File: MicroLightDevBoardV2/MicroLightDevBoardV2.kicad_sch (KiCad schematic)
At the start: 84 parts, among them J1 Conn_01x05_Socket, J10 Conn_01x02_Socket, J11 Conn_01x05_Socket, J12 Conn_01x02_Socket, J13 Conn_01x04_Socket, J14 Conn_01x04_Socket, J15 Conn_01x05_Socket, J16 Conn_01x02_Socket, J17 Conn_01x04_Socket, J18 Conn_01x02_Socket, J19 Conn_01x02_Socket, J2 Conn_01x05_Socket, J20 Conn_01x04_Socket, J21 Conn_01x04_Socket, J22 Conn_01x02_Socket, J23 Conn_01x02_Socket, J24 Conn_01x02_Socket, J25 Conn_01x02_Socket, J26 Conn_01x02_Socket, J27 Conn_01x04_Socket, J28 Conn_01x02_Socket, J29 Conn_01x04_Socket, J3 Conn_01x05_Socket, J30 Conn_01x04_Socket, J31 Conn_01x04_Socket, J32 Conn_01x04_Socket, J33 Conn_01x04_Socket, J34 Conn_01x04_Socket, J35 Conn_01x04_Socket, J36 Conn_01x04_Socket, J37 Conn_01x04_Socket, J38 Conn_01x04_Socket, J39 Conn_01x04_Socket, J4 Conn_01x05_Socket, J40 Conn_01x04_Socket, J41 Conn_01x04_Socket, J42 Conn_01x04_Socket, J43 Conn_01x04_Socket, J44 Conn_01x04_Socket, J45 Conn_01x04_Socket, J46 Conn_01x04_Socket, J47 Conn_01x04_Socket, J48 Conn_01x04_Socket, J49 Conn_01x04_Socket, J5 Conn_01x02_Socket, J50 Conn_01x04_Socket, J6 Conn_01x02_Socket, J7 TYPE-C-31-M-12, J8 Conn_01x02_Socket, J9 Conn_01x02_Socket, U1 BQ25628RYKR, U2 ATtiny3226-M, U3 S-85S1AB33-I6T1U, U4 B3U-1000P, U5 B3U-1000P, U6 USBLC6-2P6, U7 MC3479

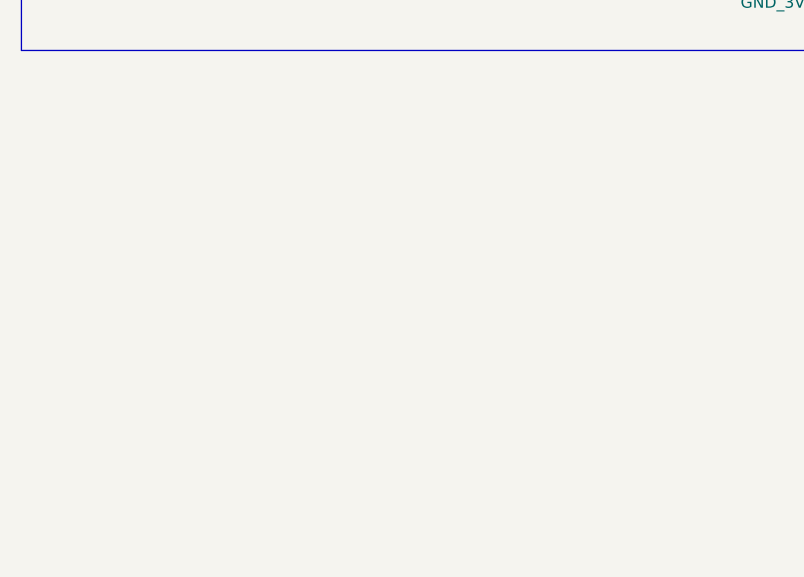
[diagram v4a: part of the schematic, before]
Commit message: added linear charging ic from TI
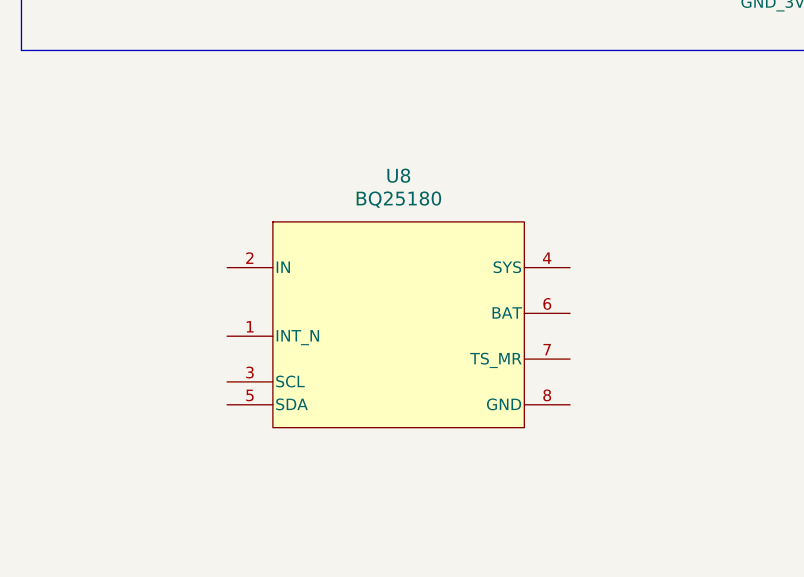
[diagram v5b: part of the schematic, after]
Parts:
- added U8: BQ25180, MicroLightDevBoard:BQ25180, symbol MicroLightDevBoard:BQ25180
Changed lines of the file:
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@@
+	)
+	(symbol
+		(lib_id "MicroLightDevBoard:BQ25180")
+		(at 38.1 213.36 0)
+		(unit 1)
+		(exclude_from_sim no)
+		(in_bom yes)
+		(on_board yes)
+		(dnp no)
+		(fields_autoplaced yes)
+		(property "Reference" "U8"
+			(at 57.15 203.2 0)
+			(effects
+				(font
+					(size 1.524 1.524)
+				)
+			)
+		)
+		(property "Value" "BQ25180"
+			(at 57.15 205.74 0)
+			(effects
+				(font
+					(size 1.524 1.524)
+				)
+			)
+		)
+		(property "Footprint" "MicroLightDevBoard:BQ25180"
+			(at 74.676 203.708 0)
+			(effects
+				(font
+					(size 1.27 1.27)
+					(italic yes)
+				)
+				(hide yes)
+			)
+		)
+		(property "Datasheet" "BQ25180"
+			(at 56.134 203.454 0)
+			(effects
+				(font
+					(size 1.27 1.27)
+					(italic yes)
+				)
+				(hide yes)
+			)
+		)
+		(property "Description" "https://www.ti.com/lit/ds/symlink/bq25180.pdf"
+			(at 57.404 198.628 0)
+			(effects
+				(font
+					(size 1.27 1.27)
+				)
+				(hide yes)
+			)
+		)
+		(pin "4"
+		)
+		(pin "7"
+		)
+		(pin "5"
+		)
+		(pin "6"
+		)
+		(pin "8"
+		)
+		(pin "3"
+		)
+		(pin "1"
+		)
+		(pin "2"
+		)
+		(instances
+			(project ""
+				(path "/4d4b60a6-56d4-4632-90b9-cd9e4f577154"
+					(reference "U8")
+					(unit 1)
+				)
+			)
+		)
 	)
 	(symbol
@@
 			)
 		)
-		(property "Datasheet" "S-85S1AB33-I6T1U"
+		(property "Datasheet" "https://www.mouser.com/datasheet/2/1490/S85S1A_E-3431038.pdf"
 			(at 57.15 168.91 0)
 			(effects

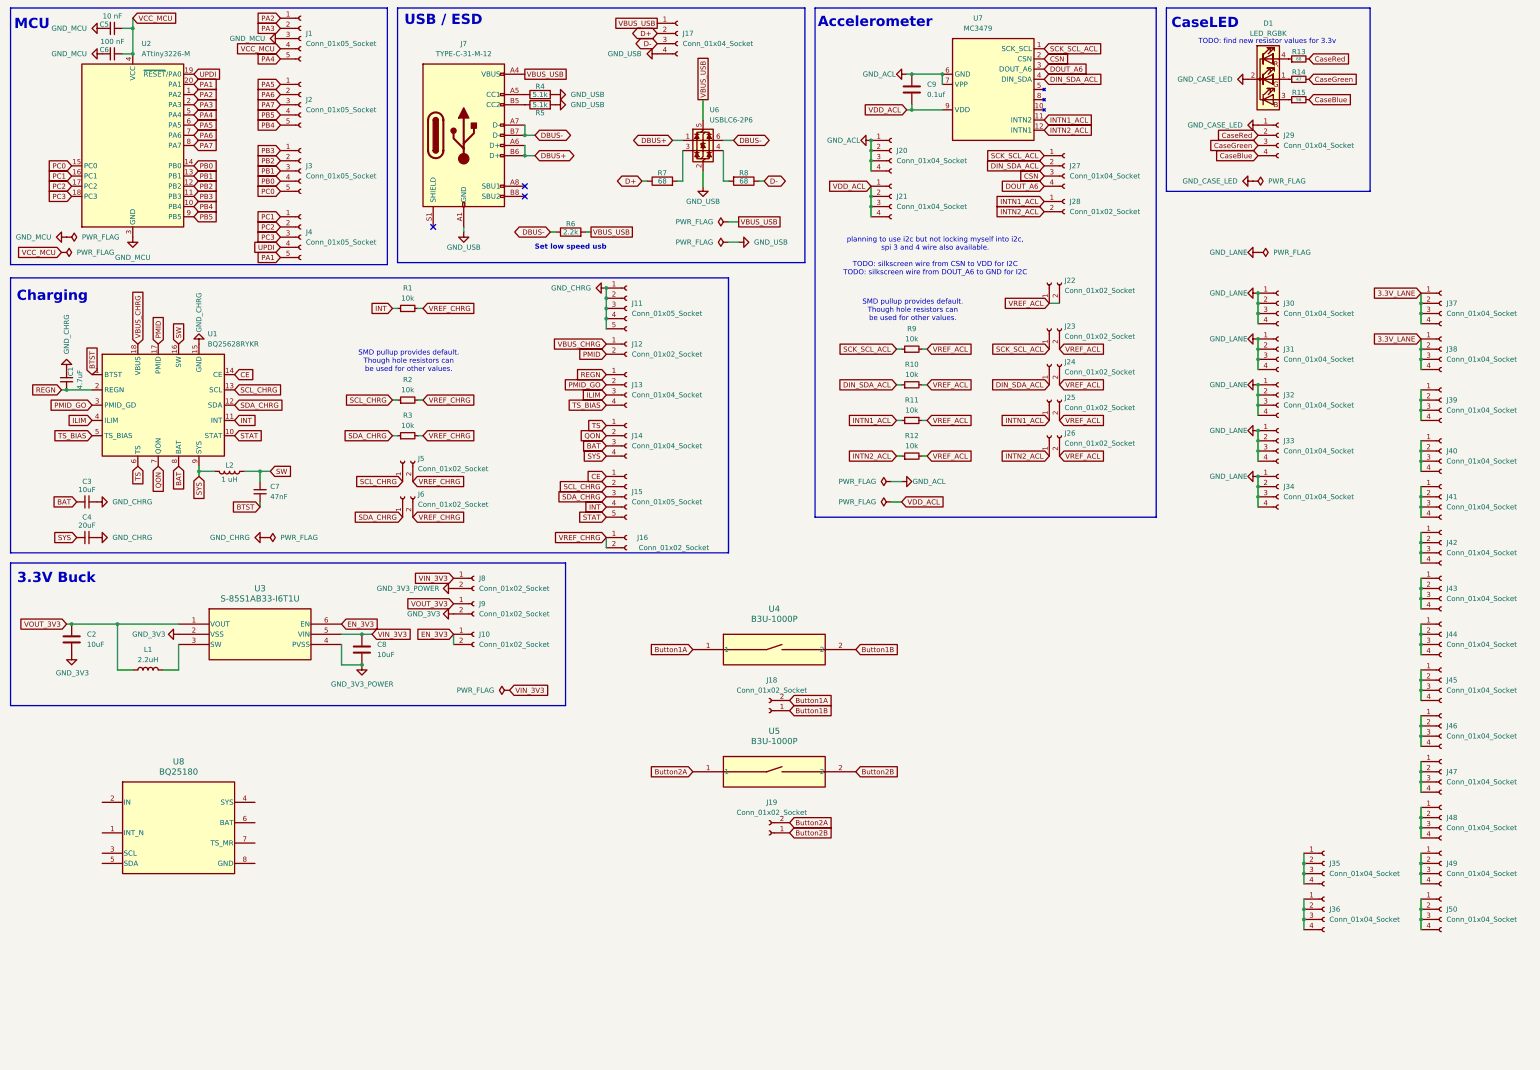
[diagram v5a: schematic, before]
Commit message: added connections for new charger ic
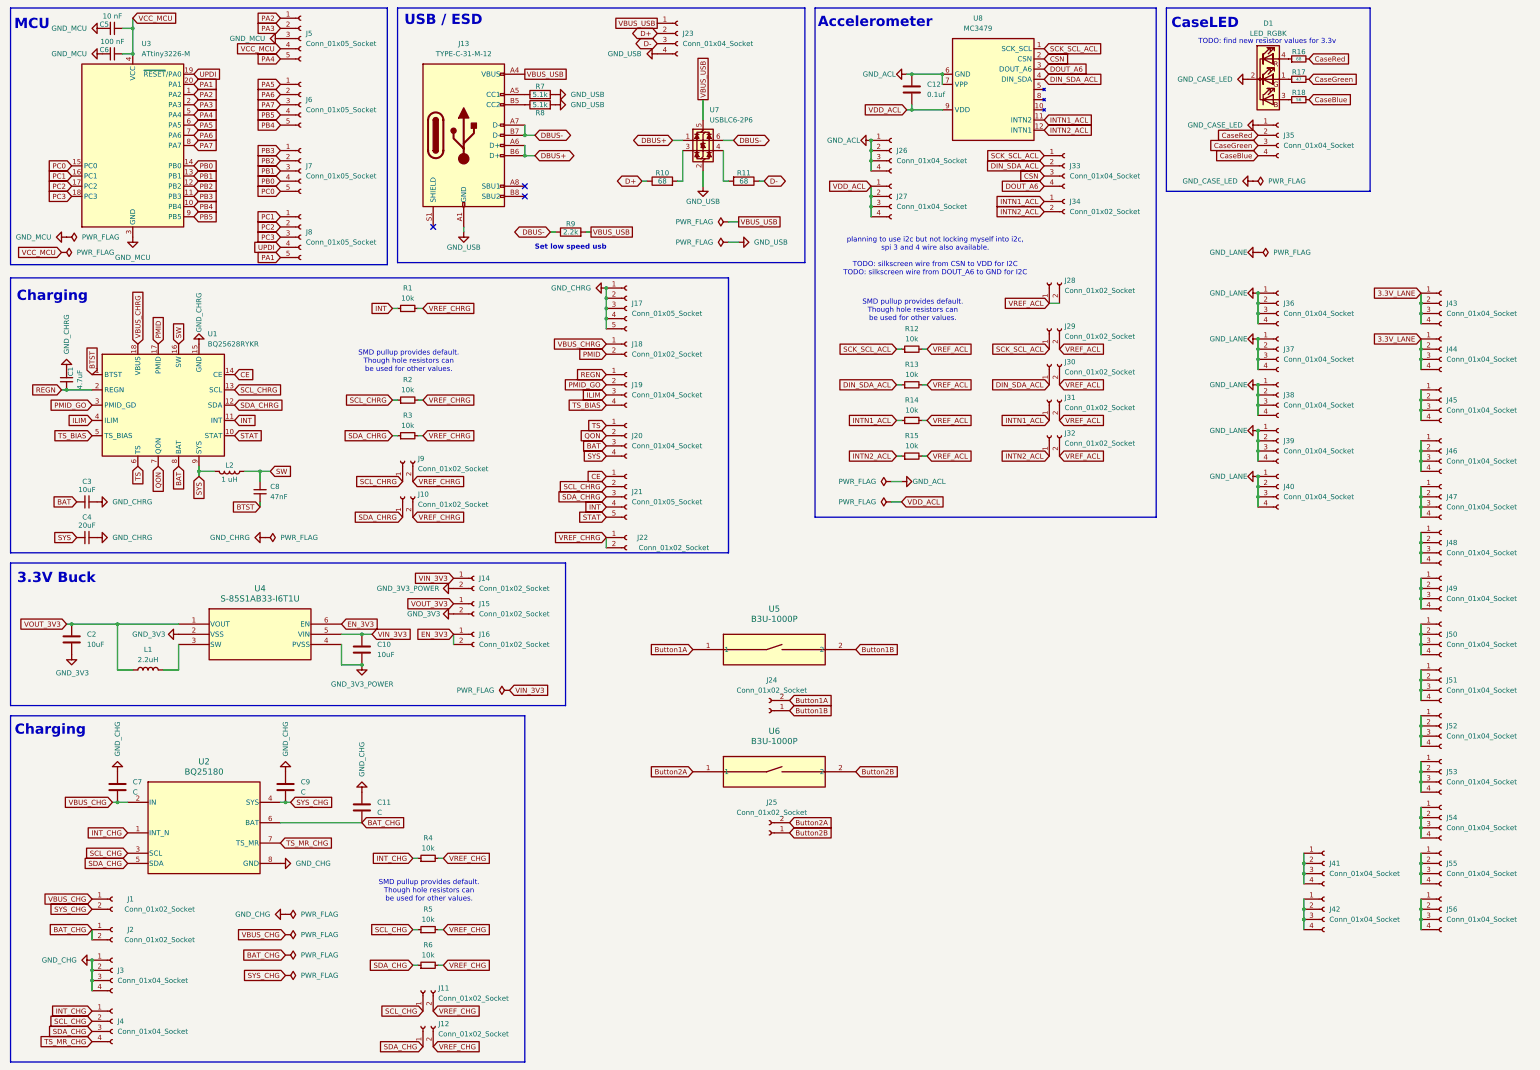
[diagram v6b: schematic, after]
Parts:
- added C11, C7, C9: C, symbol Device:C
- added J1, J11, J12, J2: Conn_01x02_Socket, Connector_PinSocket_2.54mm:PinSocket_1x02_P2.54mm_Vertical, symbol Connector:Conn_01x02_Socket
- added J3, J4: Conn_01x04_Socket, Connector_PinSocket_2.54mm:PinSocket_1x04_P2.54mm_Vertical, symbol Connector:Conn_01x04_Socket
- added R4, R5, R6: 10k, Resistor_SMD:R_0603_1608Metric, symbol Device:R_Small
- renumbered C8 to C10, C9 to C12, C7 to C8, J6 to J10, J7 to J13, J8 to J14, J9 to J15, J10 to J16, J11 to J17, J12 to J18, J13 to J19, J14 to J20, J15 to J21, J16 to J22, J17 to J23, J18 to J24, J19 to J25, J20 to J26, J21 to J27, J22 to J28, J23 to J29, J24 to J30, J25 to J31, J26 to J32, J27 to J33, J28 to J34, J29 to J35, J30 to J36, J31 to J37, J32 to J38, J33 to J39, J34 to J40, J35 to J41, J36 to J42, J37 to J43, J38 to J44, J39 to J45, J40 to J46, J41 to J47, J42 to J48, J43 to J49, J1 to J5, J44 to J50, J45 to J51, J46 to J52, J47 to J53, J48 to J54, J49 to J55, J50 to J56, J2 to J6, J3 to J7, J4 to J8, J5 to J9, R7 to R10, R8 to R11, R9 to R12, R10 to R13, R11 to R14, R12 to R15, R13 to R16, R14 to R17, R15 to R18, R4 to R7, R5 to R8, R6 to R9, U8 to U2, U2 to U3, U3 to U4, U4 to U5, U5 to U6, U6 to U7, U7 to U8
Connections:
- net INT_CHG: now reaches U2.1 (INT_N)
- net INT_CHG: now also J4.1 (Pin_1), R4.1
- net VBUS_CHG: now reaches U2.2 (IN)
- net VBUS_CHG: now also C7.2, J1.1 (Pin_1)
- net SCL_CHG: now reaches U2.3 (SCL)
- net SCL_CHG: now also J11.1 (Pin_1), J4.2 (Pin_2), R5.1
- net SYS_CHG: now reaches U2.4 (SYS)
- net SYS_CHG: now also C9.2, J1.2 (Pin_2)
- net SDA_CHG: now reaches U2.5 (SDA)
- net SDA_CHG: now also J12.1 (Pin_1), J4.3 (Pin_3), R6.1
- net BAT_CHG: now reaches U2.6 (BAT)
- net BAT_CHG: now also C11.2, J2.1 (Pin_1), J2.2 (Pin_2)
- net TS_MR_CHG: now reaches U2.7 (TS_MR)
- net TS_MR_CHG: now also J4.4 (Pin_4)
- net GND_CHG: now reaches U2.8 (GND)
- net GND_CHG: now also C11.1, C7.1, C9.1, J3.1 (Pin_1), J3.2 (Pin_2), J3.3 (Pin_3), J3.4 (Pin_4)
- new net VREF_CHG: J11.2 (Pin_2), J12.2 (Pin_2), R4.2, R5.2, R6.2
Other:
- moved on the sheet: U2

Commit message: organized new charger ic on pcb
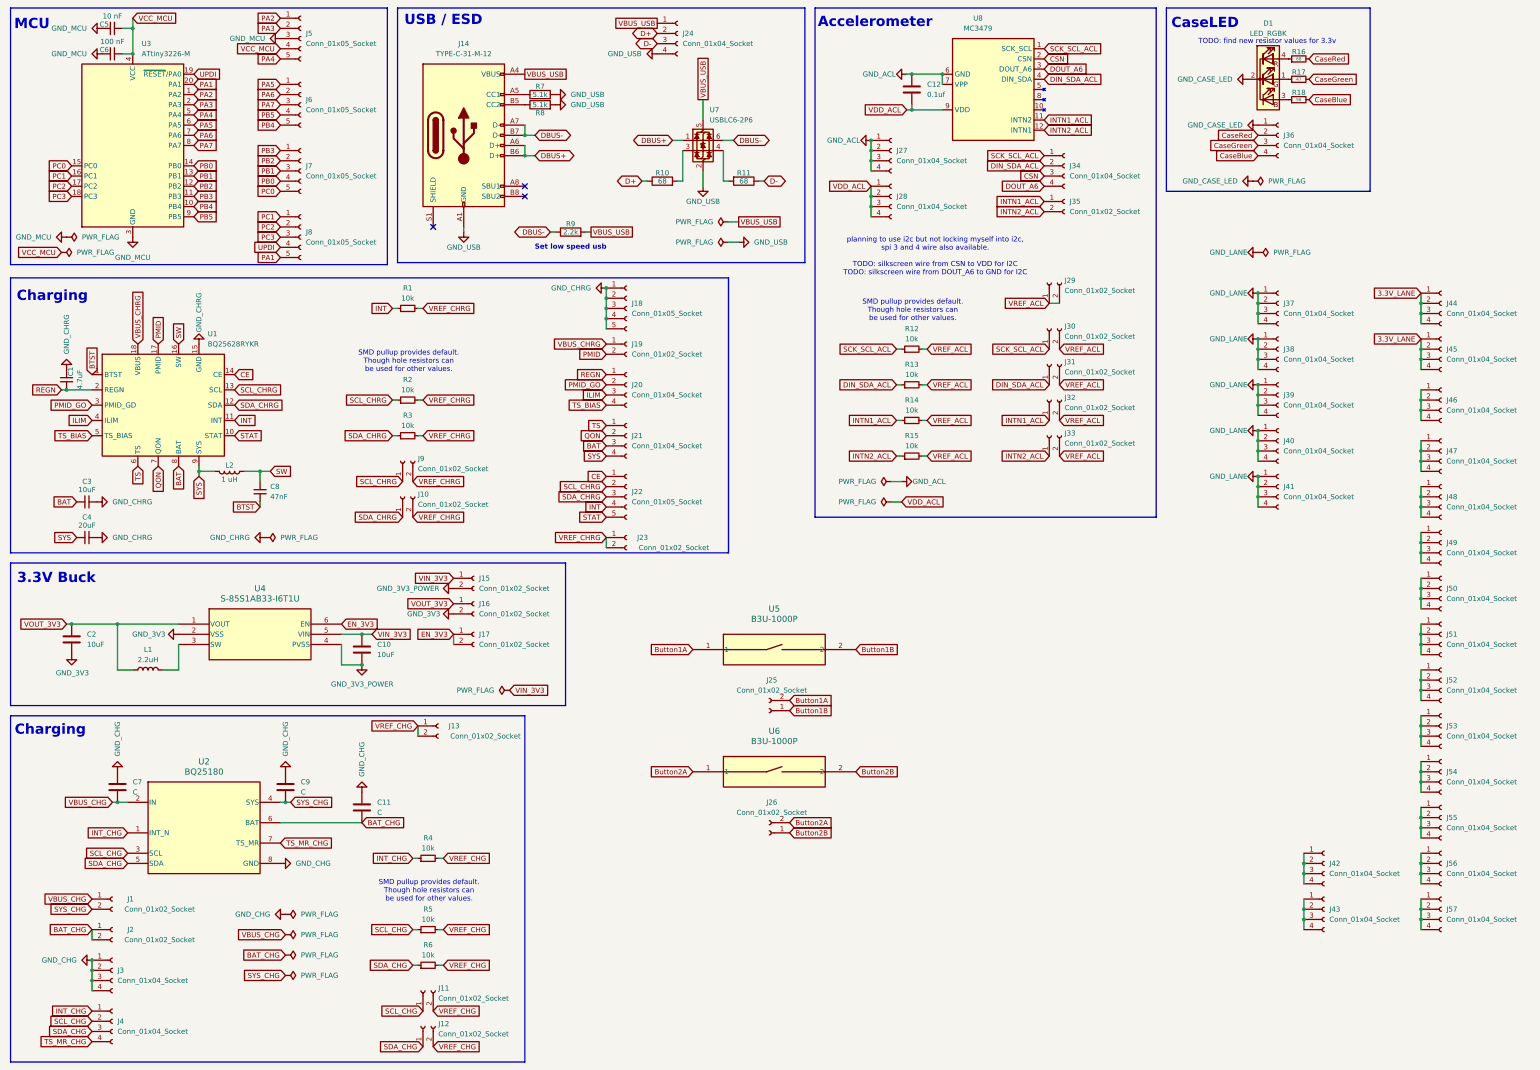
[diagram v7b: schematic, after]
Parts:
- added J13: Conn_01x02_Socket, Connector_PinSocket_2.54mm:PinSocket_1x02_P2.54mm_Vertical, symbol Connector:Conn_01x02_Socket
- renumbered J13 to J14, J14 to J15, J15 to J16, J16 to J17, J17 to J18, J18 to J19, J19 to J20, J20 to J21, J21 to J22, J22 to J23, J23 to J24, J24 to J25, J25 to J26, J26 to J27, J27 to J28, J28 to J29, J29 to J30, J30 to J31, J31 to J32, J32 to J33, J33 to J34, J34 to J35, J35 to J36, J36 to J37, J37 to J38, J38 to J39, J39 to J40, J40 to J41, J41 to J42, J42 to J43, J43 to J44, J44 to J45, J45 to J46, J46 to J47, J47 to J48, J48 to J49, J49 to J50, J50 to J51, J51 to J52, J52 to J53, J53 to J54, J54 to J55, J55 to J56, J56 to J57
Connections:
- net VREF_CHG: now also J13.1 (Pin_1), J13.2 (Pin_2)

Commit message: integrated charger ic pcb breakout into the rest of the pcb
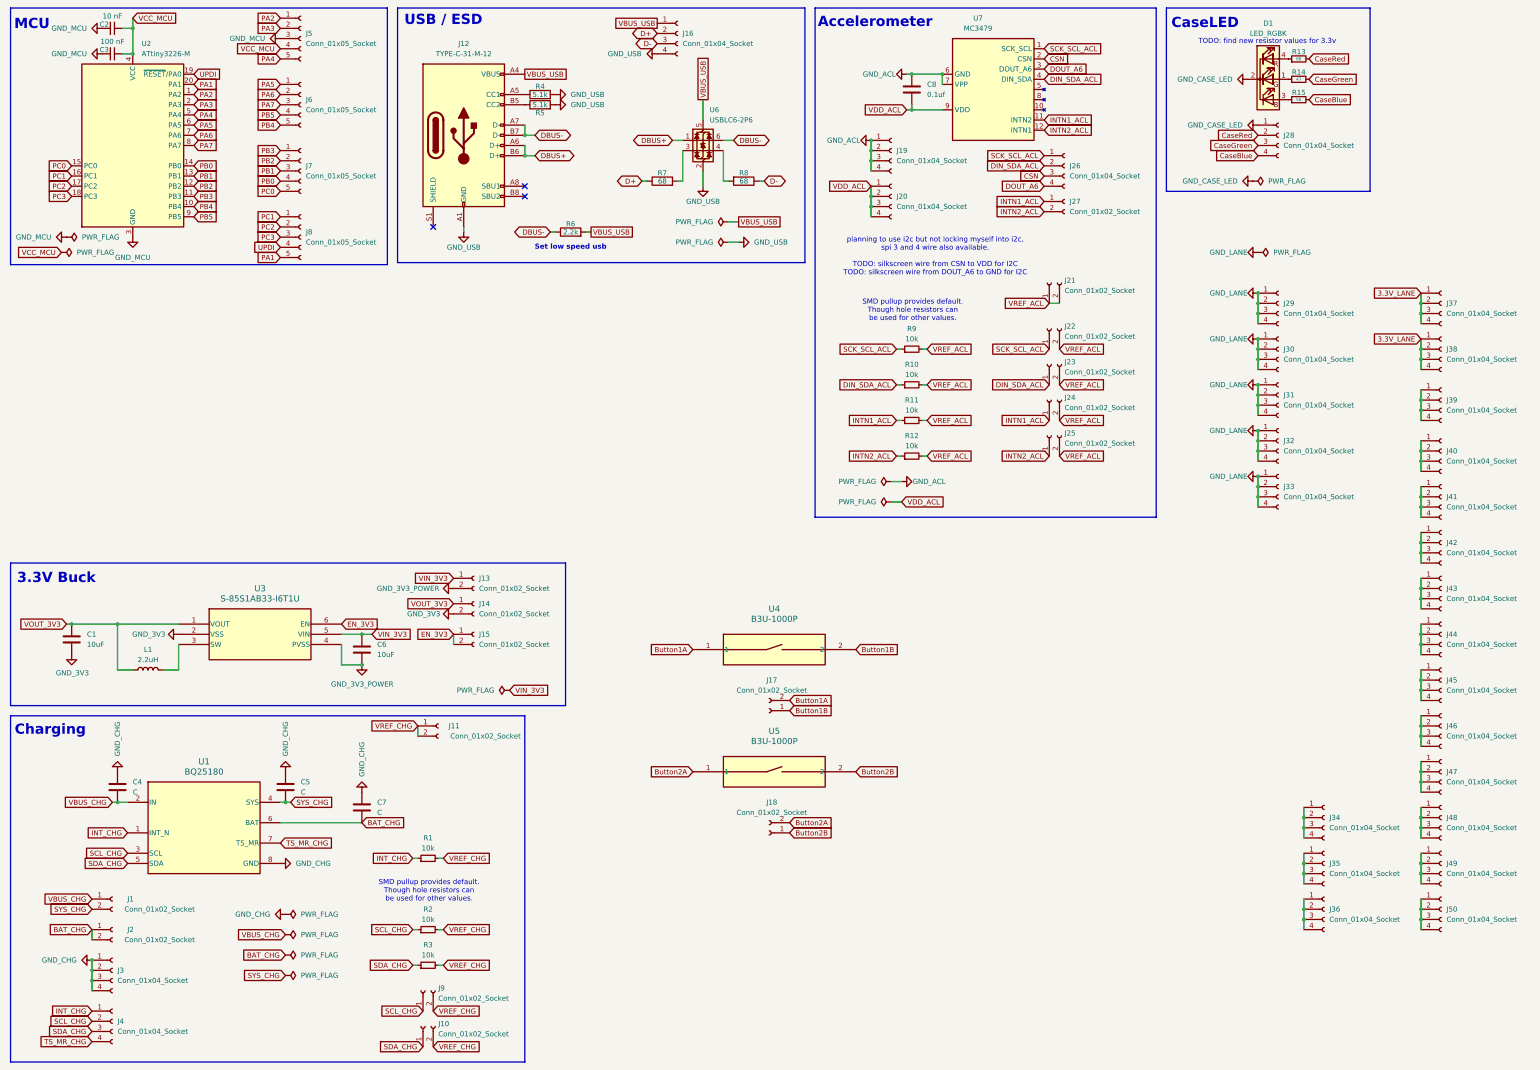
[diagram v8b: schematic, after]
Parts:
- removed C1: 4.7uF, Capacitor_SMD:C_0603_1608Metric, symbol Device:C_Small
- removed C3: 10uF, Capacitor_SMD:C_0603_1608Metric, symbol Device:C_Small
- removed C4: 20uF, Capacitor_SMD:C_0603_1608Metric, symbol Device:C_Small
- removed C8: 47nF, Capacitor_SMD:C_0603_1608Metric, symbol Device:C_Small
- removed J10, J19, J23, J9: Conn_01x02_Socket, Connector_PinSocket_2.54mm:PinSocket_1x02_P2.54mm_Vertical, symbol Connector:Conn_01x02_Socket
- removed J18, J22: Conn_01x05_Socket, Connector_PinSocket_2.54mm:PinSocket_1x05_P2.54mm_Vertical, symbol Connector:Conn_01x05_Socket
- removed J20, J21: Conn_01x04_Socket, Connector_PinSocket_2.54mm:PinSocket_1x04_P2.54mm_Vertical, symbol Connector:Conn_01x04_Socket
- removed L2: 1 uH, MicroLightDevBoard:74438322010_L, symbol Device:L
- removed R1, R2, R3: 10k, Resistor_SMD:R_0603_1608Metric, symbol Device:R_Small
- removed U1: BQ25628RYKR, MicroLightDevBoard:RYK0018A-MFG, symbol MicroLightDevBoard:BQ25628RYKR
- added J34: Conn_01x04_Socket, Connector_PinSocket_2.54mm:PinSocket_1x04_P2.54mm_Vertical, symbol Connector:Conn_01x04_Socket
- renumbered C2 to C1, C5 to C2, C6 to C3, C7 to C4, C9 to C5, C10 to C6, C11 to C7, C12 to C8, J12 to J10, J13 to J11, J14 to J12, J15 to J13, J16 to J14, J17 to J15, J24 to J16, J25 to J17, J26 to J18, J27 to J19, J28 to J20, J29 to J21, J30 to J22, J31 to J23, J32 to J24, J33 to J25, J34 to J26, J35 to J27, J36 to J28, J37 to J29, J38 to J30, J39 to J31, J40 to J32, J41 to J33, J42 to J35, J43 to J36, J44 to J37, J45 to J38, J46 to J39, J47 to J40, J48 to J41, J49 to J42, J50 to J43, J51 to J44, J52 to J45, J53 to J46, J54 to J47, J55 to J48, J56 to J49, J57 to J50, J11 to J9, R4 to R1, R13 to R10, R14 to R11, R15 to R12, R16 to R13, R17 to R14, R18 to R15, R5 to R2, R6 to R3, R7 to R4, R8 to R5, R9 to R6, R10 to R7, R11 to R8, R12 to R9, U2 to U1, U3 to U2, U4 to U3, U5 to U4, U6 to U5, U7 to U6, U8 to U7
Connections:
- new net: J34.1 (Pin_1), J34.2 (Pin_2), J34.3 (Pin_3), J34.4 (Pin_4)
